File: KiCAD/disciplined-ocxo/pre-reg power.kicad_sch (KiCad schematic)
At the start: 49 parts, among them Q1 GSFD0650, Q2 GSFD0650, U1 LM25116MHX_NOPB

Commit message: gps PCB 1.1
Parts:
- R8: value R -> 910
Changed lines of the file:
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@@
 			)
 		)
-		(property "Value" "R"
+		(property "Value" "910"
 			(at 358.14 93.9799 0)
 			(effects

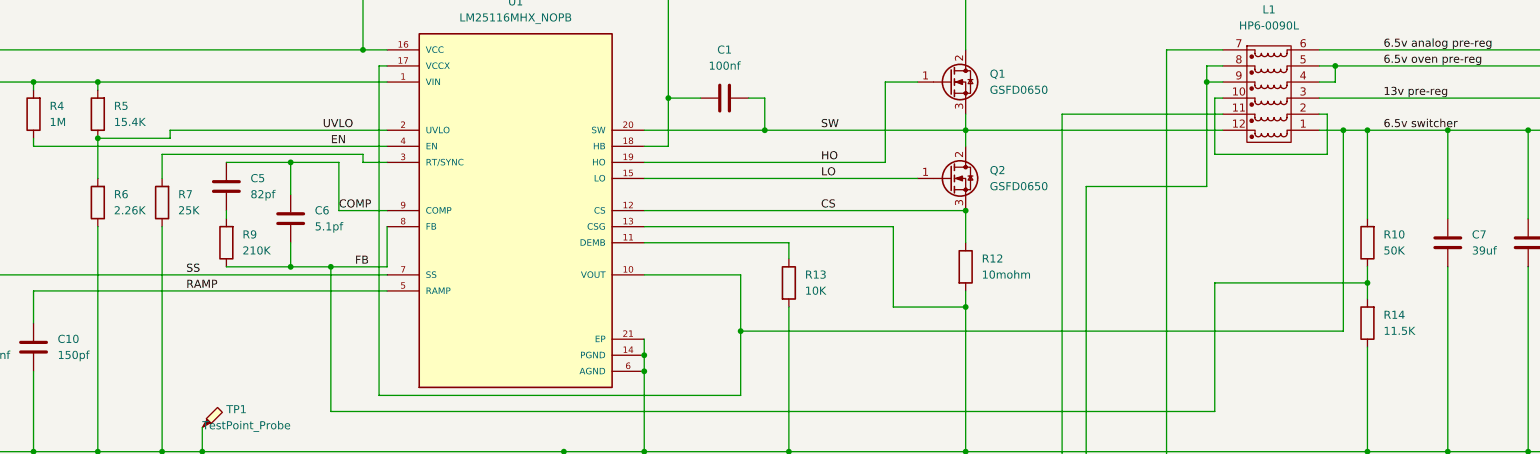
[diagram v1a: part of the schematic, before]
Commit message: ocxo board 1.1, with fixes for the major errors
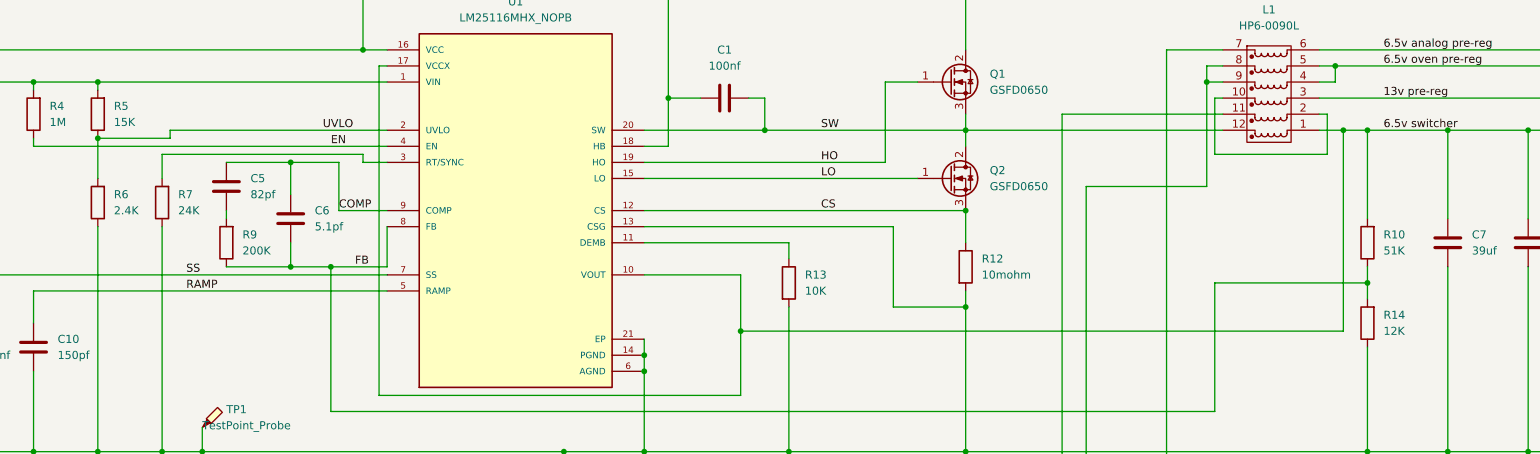
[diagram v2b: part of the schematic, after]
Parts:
- C10, C5, C6, C9: footprint Capacitor_SMD:C_0402_1005Metric_Pad0.74x0.62mm_HandSolder -> Capacitor_SMD:C_0603_1608Metric_Pad1.08x0.95mm_HandSolder
- R10: value 50K -> 51K; footprint Resistor_SMD:R_0402_1005Metric_Pad0.72x0.64mm_HandSolder -> Resistor_SMD:R_0603_1608Metric_Pad0.98x0.95mm_HandSolder
- R14: value 11.5K -> 12K; footprint Resistor_SMD:R_0402_1005Metric_Pad0.72x0.64mm_HandSolder -> Resistor_SMD:R_0603_1608Metric_Pad0.98x0.95mm_HandSolder
- R4: footprint Resistor_SMD:R_0402_1005Metric_Pad0.72x0.64mm_HandSolder -> Resistor_SMD:R_0603_1608Metric_Pad0.98x0.95mm_HandSolder
- R5: value 15.4K -> 15K; footprint Resistor_SMD:R_0402_1005Metric_Pad0.72x0.64mm_HandSolder -> Resistor_SMD:R_0603_1608Metric_Pad0.98x0.95mm_HandSolder
- R6: value 2.26K -> 2.4K; footprint Resistor_SMD:R_0402_1005Metric_Pad0.72x0.64mm_HandSolder -> Resistor_SMD:R_0603_1608Metric_Pad0.98x0.95mm_HandSolder
- R7: value 25K -> 24K; footprint Resistor_SMD:R_0402_1005Metric_Pad0.72x0.64mm_HandSolder -> Resistor_SMD:R_0603_1608Metric_Pad0.98x0.95mm_HandSolder
- R9: value 210K -> 200K; footprint Resistor_SMD:R_0402_1005Metric_Pad0.72x0.64mm_HandSolder -> Resistor_SMD:R_0603_1608Metric_Pad0.98x0.95mm_HandSolder
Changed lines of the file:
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@@
 		)
 		(instances
-			(project ""
+			(project "disciplined-ocxo"
 				(path "/524acfd4-1e59-49e3-978a-af1b55d132a7/b59c49b0-7893-4188-ac3f-f9fe9b518b62"
 					(reference "C11")
@@
 			)
 		)
-		(property "Footprint" "Capacitor_SMD:C_0402_1005Metric_Pad0.74x0.62mm_HandSolder"
+		(property "Footprint" "Capacitor_SMD:C_0603_1608Metric_Pad1.08x0.95mm_HandSolder"
 			(at 94.9452 116.84 0)
 			(effects
@@
 			)
 		)
-		(property "Value" "50K"
+		(property "Value" "51K"
 			(at 318.77 97.7899 0)
 			(effects
@@
 			)
 		)
-		(property "Footprint" "Resistor_SMD:R_0402_1005Metric_Pad0.72x0.64mm_HandSolder"
+		(property "Footprint" "Resistor_SMD:R_0603_1608Metric_Pad0.98x0.95mm_HandSolder"
 			(at 318.008 96.52 90)
 			(effects
@@
 			)
 		)
-		(property "Footprint" "Capacitor_SMD:C_0402_1005Metric_Pad0.74x0.62mm_HandSolder"
+		(property "Footprint" "Capacitor_SMD:C_0603_1608Metric_Pad1.08x0.95mm_HandSolder"
 			(at 106.3752 116.84 0)
 			(effects
@@
 			)
 		)
-		(property "Value" "15.4K"
+		(property "Value" "15K"
 			(at 118.11 77.4699 0)
 			(effects
@@
 			)
 		)
-		(property "Footprint" "Resistor_SMD:R_0402_1005Metric_Pad0.72x0.64mm_HandSolder"
+		(property "Footprint" "Resistor_SMD:R_0603_1608Metric_Pad0.98x0.95mm_HandSolder"
 			(at 117.348 76.2 90)
 			(effects
@@
 			)
 		)
-		(property "Footprint" "Capacitor_SMD:C_0402_1005Metric_Pad0.74x0.62mm_HandSolder"
+		(property "Footprint" "Capacitor_SMD:C_0603_1608Metric_Pad1.08x0.95mm_HandSolder"
 			(at 147.0152 96.52 0)
 			(effects
@@
 			)
 		)
-		(property "Value" "25K"
+		(property "Value" "24K"
 			(at 128.27 91.4399 0)
 			(effects
@@
 			)
 		)
-		(property "Footprint" "Resistor_SMD:R_0402_1005Metric_Pad0.72x0.64mm_HandSolder"
+		(property "Footprint" "Resistor_SMD:R_0603_1608Metric_Pad0.98x0.95mm_HandSolder"
 			(at 127.508 90.17 90)
 			(effects
@@
 		)
 		(instances
-			(project ""
+			(project "disciplined-ocxo"
 				(path "/524acfd4-1e59-49e3-978a-af1b55d132a7/b59c49b0-7893-4188-ac3f-f9fe9b518b62"
 					(reference "R15")
@@
 			)
 		)
-		(property "Footprint" "Capacitor_SMD:C_0402_1005Metric_Pad0.74x0.62mm_HandSolder"
+		(property "Footprint" "Capacitor_SMD:C_0603_1608Metric_Pad1.08x0.95mm_HandSolder"
 			(at 136.8552 91.44 0)
 			(effects
@@
 			)
 		)
-		(property "Value" "11.5K"
+		(property "Value" "12K"
 			(at 318.77 110.4899 0)
 			(effects
@@
 			)
 		)
-		(property "Footprint" "Resistor_SMD:R_0402_1005Metric_Pad0.72x0.64mm_HandSolder"
+		(property "Footprint" "Resistor_SMD:R_0603_1608Metric_Pad0.98x0.95mm_HandSolder"
 			(at 318.008 109.22 90)
 			(effects
@@
 			)
 		)
-		(property "Footprint" "Resistor_SMD:R_0402_1005Metric_Pad0.72x0.64mm_HandSolder"
+		(property "Footprint" "Resistor_SMD:R_0603_1608Metric_Pad0.98x0.95mm_HandSolder"
 			(at 107.188 76.2 90)
 			(effects
@@
 			)
 		)
-		(property "Value" "210K"
+		(property "Value" "200K"
 			(at 138.43 97.7899 0)
 			(effects
@@
 			)
 		)
-		(property "Footprint" "Resistor_SMD:R_0402_1005Metric_Pad0.72x0.64mm_HandSolder"
+		(property "Footprint" "Resistor_SMD:R_0603_1608Metric_Pad0.98x0.95mm_HandSolder"
 			(at 137.668 96.52 90)
 			(effects
@@
 			)
 		)
-		(property "Value" "2.26K"
+		(property "Value" "2.4K"
 			(at 118.11 91.4399 0)
 			(effects
@@
 			)
 		)
-		(property "Footprint" "Resistor_SMD:R_0402_1005Metric_Pad0.72x0.64mm_HandSolder"
+		(property "Footprint" "Resistor_SMD:R_0603_1608Metric_Pad0.98x0.95mm_HandSolder"
 			(at 117.348 90.17 90)
 			(effects

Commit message: OCXO board 1.1
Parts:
- added FID1, FID2, FID3: Fiducial, Fiducial:Fiducial_1mm_Mask3mm, symbol Mechanical:Fiducial
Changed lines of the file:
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@@
+	)
+	(symbol
+		(lib_id "Mechanical:Fiducial")
+		(at 29.21 31.75 0)
+		(unit 1)
+		(exclude_from_sim no)
+		(in_bom yes)
+		(on_board yes)
+		(dnp no)
+		(fields_autoplaced yes)
+		(property "Reference" "FID2"
+			(at 31.75 30.4799 0)
+			(effects
+				(font
+					(size 1.27 1.27)
+				)
+				(justify left)
+			)
+		)
+		(property "Value" "Fiducial"
+			(at 31.75 33.0199 0)
+			(effects
+				(font
+					(size 1.27 1.27)
+				)
+				(justify left)
+			)
+		)
+		(property "Footprint" "Fiducial:Fiducial_1mm_Mask3mm"
+			(at 29.21 31.75 0)
+			(effects
+				(font
+					(size 1.27 1.27)
+				)
+				(hide yes)
+			)
+		)
+		(property "Datasheet" "~"
+			(at 29.21 31.75 0)
+			(effects
+				(font
+					(size 1.27 1.27)
+				)
+				(hide yes)
+			)
+		)
+		(property "Description" "Fiducial Marker"
+			(at 29.21 31.75 0)
+			(effects
+				(font
+					(size 1.27 1.27)
+				)
+				(hide yes)
+			)
+		)
+		(instances
+			(project "disciplined-ocxo"
+				(path "/524acfd4-1e59-49e3-978a-af1b55d132a7/b59c49b0-7893-4188-ac3f-f9fe9b518b62"
+					(reference "FID2")
+					(unit 1)
+				)
+			)
+		)
 	)
 	(symbol
@@
 				(path "/524acfd4-1e59-49e3-978a-af1b55d132a7/b59c49b0-7893-4188-ac3f-f9fe9b518b62"
 					(reference "R5")
+					(unit 1)
+				)
+			)
+		)
+	)
+	(symbol
+		(lib_id "Mechanical:Fiducial")
+		(at 29.21 38.1 0)
+		(unit 1)
+		(exclude_from_sim no)
+		(in_bom yes)
+		(on_board yes)
+		(dnp no)
+		(fields_autoplaced yes)
+		(property "Reference" "FID3"
+			(at 31.75 36.8299 0)
+			(effects
+				(font
+					(size 1.27 1.27)
+				)
+				(justify left)
+			)
+		)
+		(property "Value" "Fiducial"
+			(at 31.75 39.3699 0)
+			(effects
+				(font
+					(size 1.27 1.27)
+				)
+				(justify left)
+			)
+		)
+		(property "Footprint" "Fiducial:Fiducial_1mm_Mask3mm"
+			(at 29.21 38.1 0)
+			(effects
+				(font
+					(size 1.27 1.27)
+				)
+				(hide yes)
+			)
+		)
+		(property "Datasheet" "~"
+			(at 29.21 38.1 0)
+			(effects
+				(font
+					(size 1.27 1.27)
+				)
+				(hide yes)
+			)
+		)
+		(property "Description" "Fiducial Marker"
+			(at 29.21 38.1 0)
+			(effects
+				(font
+					(size 1.27 1.27)
+				)
+				(hide yes)
+			)
+		)
+		(instances
+			(project "disciplined-ocxo"
+				(path "/524acfd4-1e59-49e3-978a-af1b55d132a7/b59c49b0-7893-4188-ac3f-f9fe9b518b62"
+					(reference "FID3")
 					(unit 1)
 				)
@@
 					(unit 1)
 				)
+			)
+		)
+	)
+	(symbol
+		(lib_id "Mechanical:Fiducial")
+		(at 29.21 25.4 0)
+		(unit 1)
+		(exclude_from_sim no)
+		(in_bom yes)
+		(on_board yes)
+		(dnp no)
+		(fields_autoplaced yes)
+		(property "Reference" "FID1"
+			(at 31.75 24.1299 0)
+			(effects
+				(font
+					(size 1.27 1.27)
+				)
+				(justify left)
+			)
+		)
+		(property "Value" "Fiducial"
+			(at 31.75 26.6699 0)
+			(effects
+				(font
+					(size 1.27 1.27)
+				)
+				(justify left)
+			)
+		)
+		(property "Footprint" "Fiducial:Fiducial_1mm_Mask3mm"
+			(at 29.21 25.4 0)
+			(effects
+				(font
+					(size 1.27 1.27)
+				)
+				(hide yes)
+			)
+		)
+		(property "Datasheet" "~"
+			(at 29.21 25.4 0)
+			(effects
+				(font
+					(size 1.27 1.27)
+				)
+				(hide yes)
+			)
+		)
+		(property "Description" "Fiducial Marker"
+			(at 29.21 25.4 0)
+			(effects
+				(font
+					(size 1.27 1.27)
+				)
+				(hide yes)
+			)
+		)
+		(instances
+			(project "disciplined-ocxo"
+				(path "/524acfd4-1e59-49e3-978a-af1b55d132a7/b59c49b0-7893-4188-ac3f-f9fe9b518b62"
+					(reference "FID1")
+					(unit 1)
+				)

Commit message: LDO daughterboard 1.1
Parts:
- added U15, U16: LT8302ES8E-3-PBF, ! Analog Devices:05-08-1857_ADI, symbol ! Analog Devices:LT8302ES8E-3-PBF
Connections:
- net 12V IN: now also U15.3 (VIN), U16.3 (VIN); no longer C2.1, C3.1, R4.2, R5.2, U1.1 (VIN)
- new net: C2.1, C3.1, R4.2, R5.2, U1.1 (VIN)
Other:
- moved on the sheet: C1, C10, C11, C12, C13, C14, C15, C16, C17, C18, C19, C2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
